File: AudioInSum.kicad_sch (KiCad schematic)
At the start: 18 parts, among them U7 TLV9062IDR

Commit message: started layout
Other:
- moved on the sheet: R25
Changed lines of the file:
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@@
   (junction (at 119.38 180.34) (diameter 0) (color 0 0 0 0)
   )
-  (junction (at 170.18 56.515) (diameter 0) (color 0 0 0 0)
-  )
   (junction (at 130.175 53.975) (diameter 0) (color 0 0 0 0)
   )
+  (junction (at 170.815 107.95) (diameter 0) (color 0 0 0 0)
+  )
   (junction (at 130.175 102.87) (diameter 0) (color 0 0 0 0)
   )
   (junction (at 114.3 102.87) (diameter 0) (color 0 0 0 0)
   )
-  (junction (at 149.86 118.11) (diameter 0) (color 0 0 0 0)
-  )
   (junction (at 128.905 102.87) (diameter 0) (color 0 0 0 0)
   )
-  (junction (at 169.545 107.95) (diameter 0) (color 0 0 0 0)
-  )
   (junction (at 108.585 53.975) (diameter 0) (color 0 0 0 0)
   )
@@
   (junction (at 119.38 147.32) (diameter 0) (color 0 0 0 0)
   )
+  (junction (at 172.72 56.515) (diameter 0) (color 0 0 0 0)
+  )
+  (junction (at 148.59 118.11) (diameter 0) (color 0 0 0 0)
+  )
   (junction (at 148.59 63.5) (diameter 0) (color 0 0 0 0)
   )
@@
     (stroke (width 0) (type default))
   )
-  (wire (pts (xy 118.11 147.32) (xy 119.38 147.32))
-    (stroke (width 0) (type default))
-  )
   (wire (pts (xy 148.59 55.88) (xy 149.86 55.88))
     (stroke (width 0) (type default))
@@
     (stroke (width 0) (type default))
   )
-  (wire (pts (xy 170.18 56.515) (xy 175.26 56.515))
+  (wire (pts (xy 170.815 107.95) (xy 174.625 107.95))
     (stroke (width 0) (type default))
   )
@@
     (stroke (width 0) (type default))
   )
-  (wire (pts (xy 149.86 118.11) (xy 148.59 118.11))
+  (wire (pts (xy 148.59 118.11) (xy 154.94 118.11))
     (stroke (width 0) (type default))
   )
@@
     (stroke (width 0) (type default))
   )
-  (wire (pts (xy 169.545 107.95) (xy 169.545 118.11))
+  (wire (pts (xy 170.815 107.95) (xy 170.815 118.11))
     (stroke (width 0) (type default))
   )
@@
     (stroke (width 0) (type default))
   )
-  (wire (pts (xy 133.35 180.34) (xy 119.38 180.34))
+  (wire (pts (xy 119.38 180.34) (xy 143.51 180.34))
     (stroke (width 0) (type default))
   )
@@
     (stroke (width 0) (type default))
   )
-  (wire (pts (xy 170.18 53.34) (xy 170.18 56.515))
-    (stroke (width 0) (type default))
-  )
   (wire (pts (xy 119.38 180.34) (xy 119.38 176.53))
     (stroke (width 0) (type default))
@@
     (stroke (width 0) (type default))
   )
-  (wire (pts (xy 169.545 118.11) (xy 162.56 118.11))
-    (stroke (width 0) (type default))
-  )
-  (wire (pts (xy 132.715 153.67) (xy 143.51 153.67))
+  (wire (pts (xy 170.815 118.11) (xy 162.56 118.11))
+    (stroke (width 0) (type default))
+  )
+  (wire (pts (xy 172.72 56.515) (xy 175.26 56.515))
     (stroke (width 0) (type default))
   )
@@
     (stroke (width 0) (type default))
   )
-  (wire (pts (xy 143.51 173.99) (xy 143.51 167.64))
+  (wire (pts (xy 143.51 180.34) (xy 143.51 167.64))
     (stroke (width 0) (type default))
   )
@@
     (stroke (width 0) (type default))
   )
-  (wire (pts (xy 170.18 63.5) (xy 162.56 63.5))
-    (stroke (width 0) (type default))
-  )
-  (wire (pts (xy 149.86 128.27) (xy 149.86 127))
-    (stroke (width 0) (type default))
-  )
-  (wire (pts (xy 169.545 107.95) (xy 168.91 107.95))
+  (wire (pts (xy 172.72 63.5) (xy 162.56 63.5))
+    (stroke (width 0) (type default))
+  )
+  (wire (pts (xy 148.59 128.27) (xy 148.59 127))
     (stroke (width 0) (type default))
   )
@@
     (stroke (width 0) (type default))
   )
-  (wire (pts (xy 168.91 105.41) (xy 168.91 107.95))
+  (wire (pts (xy 170.815 105.41) (xy 170.815 107.95))
     (stroke (width 0) (type default))
   )
@@
     (stroke (width 0) (type default))
   )
-  (wire (pts (xy 132.715 153.67) (xy 132.715 147.32))
-    (stroke (width 0) (type default))
-  )
   (wire (pts (xy 103.505 41.91) (xy 108.585 41.91))
     (stroke (width 0) (type default))
   )
+  (wire (pts (xy 172.72 53.34) (xy 172.72 56.515))
+    (stroke (width 0) (type default))
+  )
   (wire (pts (xy 114.3 102.87) (xy 114.3 105.41))
     (stroke (width 0) (type default))
   )
-  (wire (pts (xy 132.715 147.32) (xy 119.38 147.32))
-    (stroke (width 0) (type default))
-  )
-  (wire (pts (xy 169.545 107.95) (xy 174.625 107.95))
+  (wire (pts (xy 119.38 147.32) (xy 143.51 147.32))
     (stroke (width 0) (type default))
   )
@@
     (stroke (width 0) (type default))
   )
-  (wire (pts (xy 133.35 173.99) (xy 133.35 180.34))
-    (stroke (width 0) (type default))
-  )
   (wire (pts (xy 121.285 53.975) (xy 130.175 53.975))
     (stroke (width 0) (type default))
   )
+  (wire (pts (xy 172.72 53.34) (xy 170.18 53.34))
+    (stroke (width 0) (type default))
+  )
   (wire (pts (xy 119.38 147.32) (xy 119.38 151.13))
     (stroke (width 0) (type default))
@@
     (stroke (width 0) (type default))
   )
-  (wire (pts (xy 143.51 153.67) (xy 143.51 160.02))
-    (stroke (width 0) (type default))
-  )
-  (wire (pts (xy 154.94 118.11) (xy 149.86 118.11))
-    (stroke (width 0) (type default))
-  )
-  (wire (pts (xy 170.18 56.515) (xy 170.18 63.5))
+  (wire (pts (xy 143.51 147.32) (xy 143.51 160.02))
+    (stroke (width 0) (type default))
+  )
+  (wire (pts (xy 172.72 56.515) (xy 172.72 63.5))
     (stroke (width 0) (type default))
   )
@@
     (stroke (width 0) (type default))
   )
-  (wire (pts (xy 149.86 118.11) (xy 149.86 119.38))
+  (wire (pts (xy 170.815 105.41) (xy 168.91 105.41))
+    (stroke (width 0) (type default))
+  )
+  (wire (pts (xy 148.59 118.11) (xy 148.59 119.38))
     (stroke (width 0) (type default))
   )
@@
     (stroke (width 0) (type default))
   )
-  (wire (pts (xy 118.11 144.78) (xy 118.11 147.32))
+  (wire (pts (xy 119.38 144.78) (xy 119.38 147.32))
     (stroke (width 0) (type default))
   )
@@
   )
   (wire (pts (xy 128.905 115.57) (xy 128.905 113.03))
-    (stroke (width 0) (type default))
-  )
-  (wire (pts (xy 133.35 173.99) (xy 143.51 173.99))
     (stroke (width 0) (type default))
   )
@@
     (effects (font (size 1.27 1.27)) (justify left))
   )
-  (hierarchical_label "VCC" (shape input) (at 118.11 144.78 90) (fields_autoplaced)
+  (hierarchical_label "VCC" (shape input) (at 119.38 144.78 90) (fields_autoplaced)
     (effects (font (size 1.27 1.27)) (justify left))
   )
@@
     )
   )
-  (symbol (lib_id "power:GND") (at 149.86 128.27 0) (unit 1)
-    (in_bom yes) (on_board yes) (dnp no)
-    (property "Reference" "#PWR011" (at 149.86 134.62 0)
-      (effects (font (size 1.27 1.27)) hide)
-    )
-    (property "Value" "GND" (at 154.305 128.27 0)
-      (effects (font (size 1.27 1.27)))
-    )
-    (property "Footprint" "" (at 149.86 128.27 0)
-      (effects (font (size 1.27 1.27)) hide)
-    )
-    (property "Datasheet" "" (at 149.86 128.27 0)
+  (symbol (lib_id "power:GND") (at 148.59 128.27 0) (unit 1)
+    (in_bom yes) (on_board yes) (dnp no)
+    (property "Reference" "#PWR011" (at 148.59 134.62 0)
+      (effects (font (size 1.27 1.27)) hide)
+    )
+    (property "Value" "GND" (at 153.035 128.27 0)
+      (effects (font (size 1.27 1.27)))
+    )
+    (property "Footprint" "" (at 148.59 128.27 0)
+      (effects (font (size 1.27 1.27)) hide)
+    )
+    (property "Datasheet" "" (at 148.59 128.27 0)
       (effects (font (size 1.27 1.27)) hide)
     )
@@
     )
   )
-  (symbol (lib_id "Device:R_US") (at 149.86 123.19 0) (unit 1)
-    (in_bom yes) (on_board yes) (dnp no)
-    (property "Reference" "R25" (at 153.67 122.555 90)
-      (effects (font (size 1.27 1.27)))
-    )
-    (property "Value" "DNP" (at 151.765 122.555 90)
-      (effects (font (size 1.27 1.27)))
-    )
-    (property "Footprint" "Resistor_SMD:R_0402_1005Metric" (at 150.876 123.444 90)
-      (effects (font (size 1.27 1.27)) hide)
-    )
-    (property "Datasheet" "~" (at 149.86 123.19 0)
-      (effects (font (size 1.27 1.27)) hide)
-    )
-    (property "Specks" "0402" (at 151.765 119.38 90)
-      (effects (font (size 1.27 1.27)) hide)
-    )
+  (symbol (lib_id "Device:R_US") (at 148.59 123.19 0) (unit 1)
+    (in_bom yes) (on_board yes) (dnp no)
+    (property "Reference" "R25" (at 152.4 122.555 90)
+      (effects (font (size 1.27 1.27)))
+    )
+    (property "Value" "DNP" (at 150.495 122.555 90)
+      (effects (font (size 1.27 1.27)))
+    )
+    (property "Footprint" "Resistor_SMD:R_0402_1005Metric" (at 149.606 123.444 90)
+      (effects (font (size 1.27 1.27)) hide)
+    )
+    (property "Datasheet" "~" (at 148.59 123.19 0)
+      (effects (font (size 1.27 1.27)) hide)
+    )
+    (property "Specks" "0402" (at 150.495 119.38 90)
+      (effects (font (size 1.27 1.27)) hide)
+    )

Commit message: periodic update
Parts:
- removed C11 (x2): 10U, Capacitor_SMD:C_0805_2012Metric, symbol Device:C
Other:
- note added: "Audio In"
- note removed: "Audio In Sum and Rebuffer"
- moved on the sheet: R8

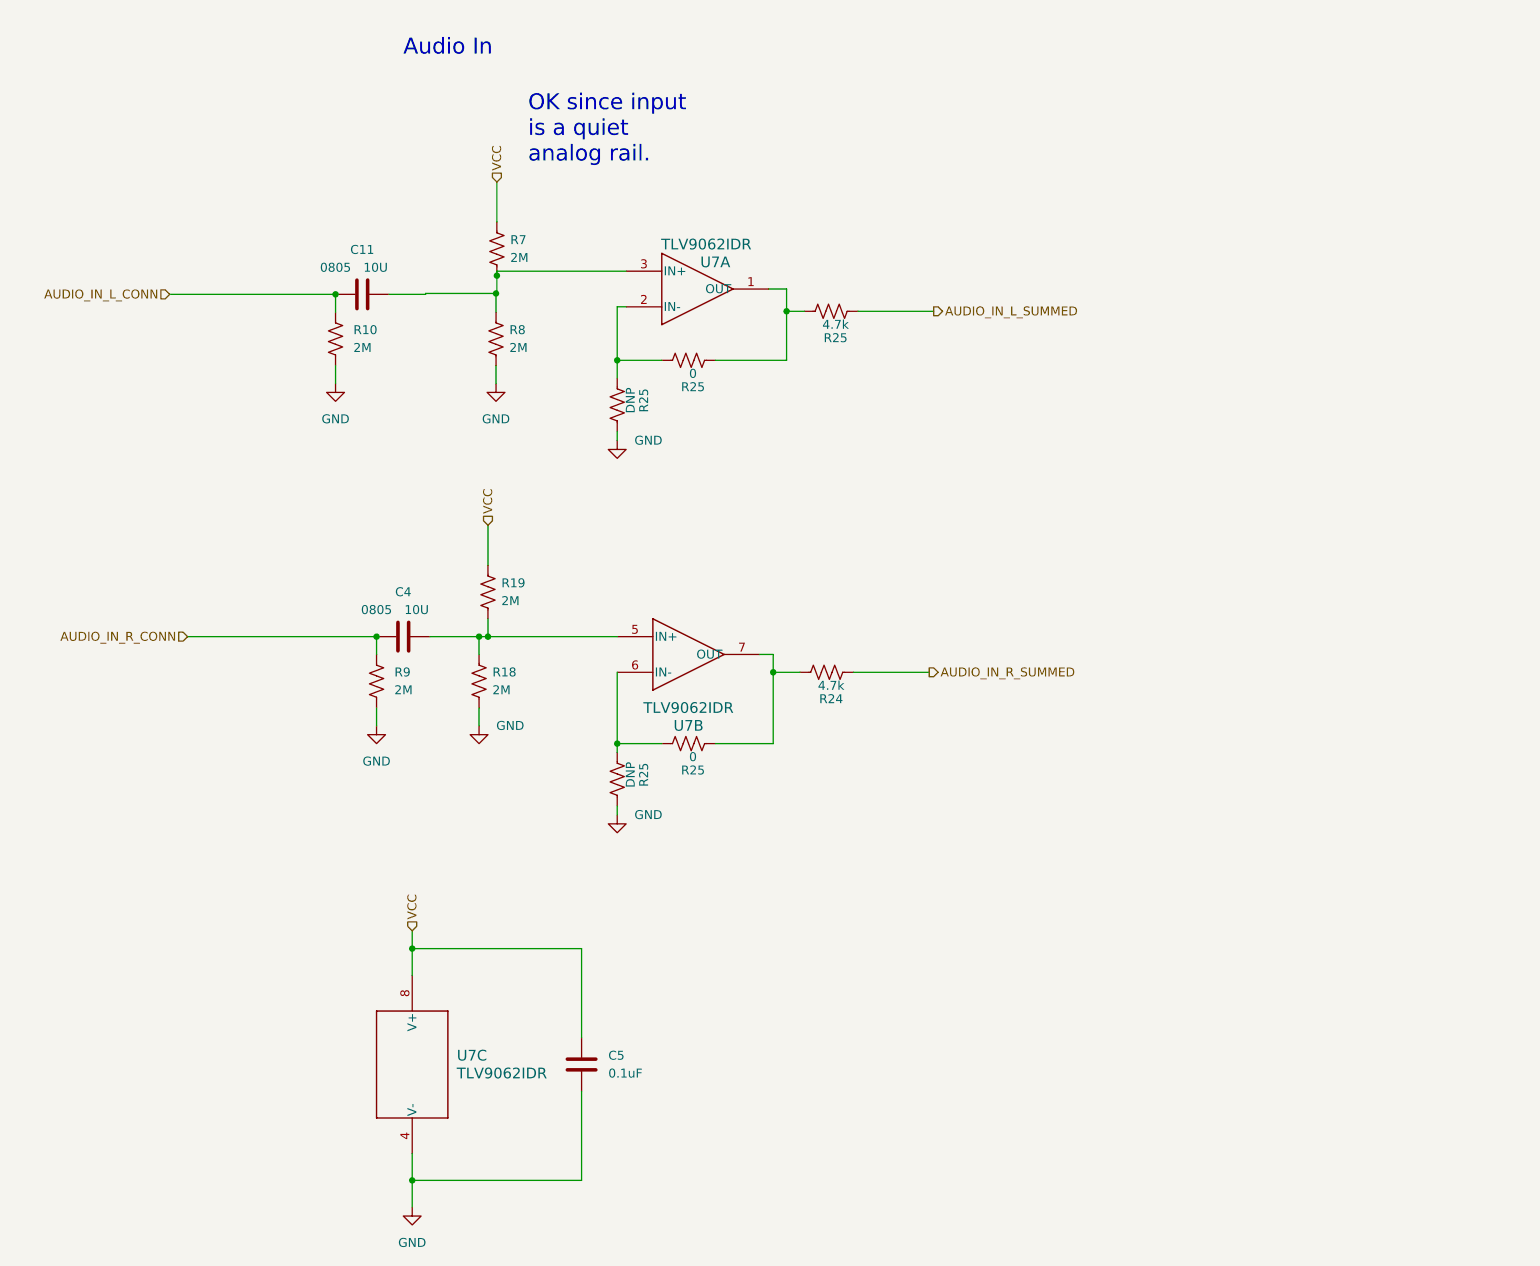
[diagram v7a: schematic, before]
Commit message: added dedicated SPI, UART, I2C connectors
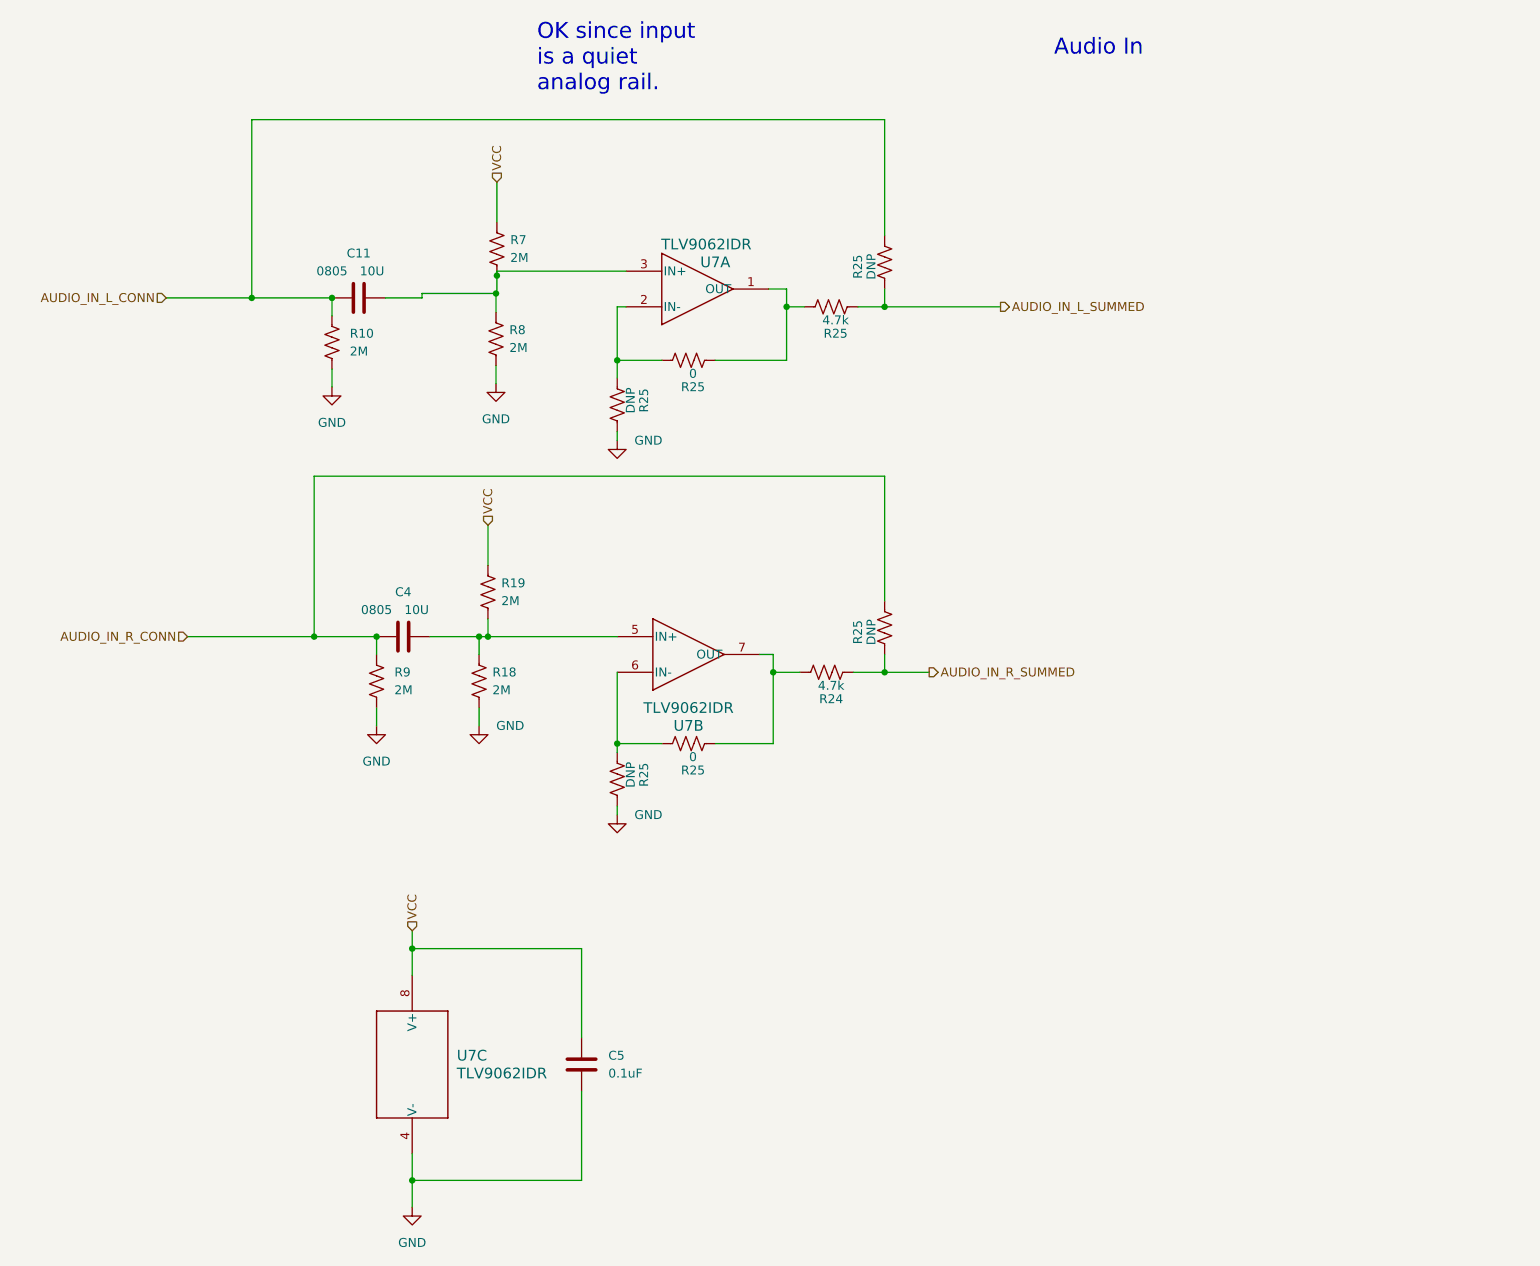
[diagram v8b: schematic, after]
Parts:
- added R25 (x2): DNP, Resistor_SMD:R_0402_1005Metric, symbol Device:R_US
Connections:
- net AUDIO_IN_L_CONN: now also R25.2
- net AUDIO_IN_L_SUMMED: now also R25.1
- net AUDIO_IN_R_CONN: now also R25.2
- net AUDIO_IN_R_SUMMED: now also R25.1
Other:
- moved on the sheet: C11, R10, R25
